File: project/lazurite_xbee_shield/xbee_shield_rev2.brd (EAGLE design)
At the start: 23 x 32.2 mm, 2 parts

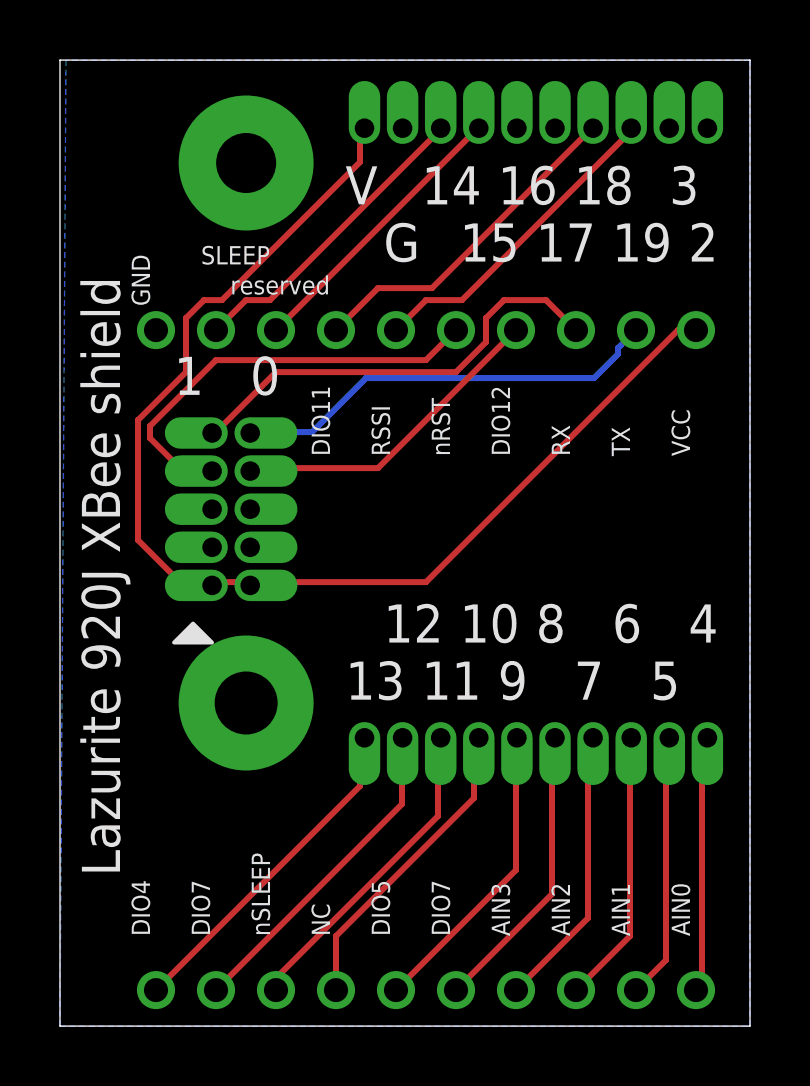
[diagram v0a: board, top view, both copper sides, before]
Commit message: update libraries and all schematic/board data.
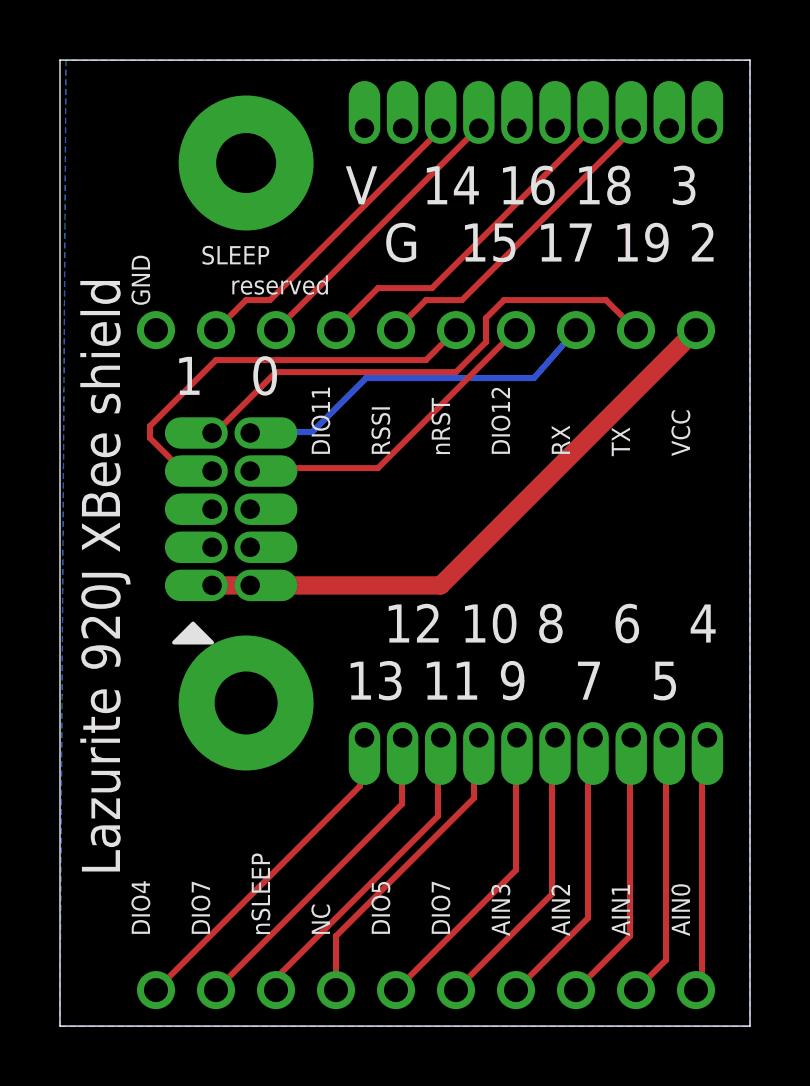
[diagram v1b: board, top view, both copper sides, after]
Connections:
- net 0: now also XB1.3; no longer XB1.2
- net 1: now also XB1.2; no longer XB1.3
- net VDD: no longer U1.VCC3V_2
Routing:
- net VDD: track 40.1 -> 19.7 mm
- net 0: track 14.4 -> 12.3 mm
- net 1: track 14.8 -> 16.8 mm
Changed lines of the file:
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@@
 </signal>
 <signal name="0">
-<contactref element="XB1" pad="2"/>
 <contactref element="U1" pad="0"/>
 <wire x1="8.4" y1="19.8" x2="6.4" y2="19.8" width="0.2" layer="16"/>
 <wire x1="10.2" y1="21.6" x2="8.4" y2="19.8" width="0.2" layer="16"/>
-<wire x1="17.8" y1="21.6" x2="10.2" y2="21.6" width="0.2" layer="16"/>
-<wire x1="18.6" y1="22.4" x2="17.8" y2="21.6" width="0.2" layer="16"/>
-<wire x1="18.6" y1="22.6" x2="18.6" y2="22.4" width="0.2" layer="16"/>
-<wire x1="19.2" y1="23.2" x2="18.6" y2="22.6" width="0.2" layer="16"/>
+<wire x1="15.8" y1="21.6" x2="10.2" y2="21.6" width="0.2" layer="16"/>
 <wire x1="6.4" y1="19.8" x2="6.34" y2="19.77" width="0.2" layer="16"/>
+<contactref element="XB1" pad="3"/>
+<wire x1="15.8" y1="21.6" x2="17.2" y2="23.2" width="0.2" layer="16"/>
 </signal>
 <signal name="1">
-<contactref element="XB1" pad="3"/>
 <contactref element="U1" pad="1"/>
 <wire x1="7.2" y1="21.8" x2="5.2" y2="19.8" width="0.2" layer="1"/>
@@
 <wire x1="14.2" y1="23.6" x2="14.2" y2="22.8" width="0.2" layer="1"/>
 <wire x1="14.8" y1="24.2" x2="14.2" y2="23.6" width="0.2" layer="1"/>
-<wire x1="16.2" y1="24.2" x2="14.8" y2="24.2" width="0.2" layer="1"/>
-<wire x1="17.2" y1="23.2" x2="16.2" y2="24.2" width="0.2" layer="1"/>
+<wire x1="18.2" y1="24.2" x2="14.8" y2="24.2" width="0.2" layer="1"/>
 <wire x1="5.2" y1="19.8" x2="5.07" y2="19.77" width="0.2" layer="1"/>
+<contactref element="XB1" pad="2"/>
+<wire x1="18.2" y1="24.2" x2="19.2" y2="23.2" width="0.2" layer="1"/>
 </signal>
 <signal name="TEST1N">
@@
 <contactref element="XB1" pad="1"/>
 <contactref element="U1" pad="VCC5V_1"/>
-<contactref element="U1" pad="VCC3V_2"/>
-<wire x1="6.2" y1="14.8" x2="5.2" y2="14.8" width="0.2" layer="1"/>
-<wire x1="5.2" y1="14.8" x2="5.07" y2="14.69" width="0.2" layer="1"/>
-<wire x1="6.2" y1="14.8" x2="6.34" y2="14.69" width="0.2" layer="1"/>
-<wire x1="10" y1="28.8" x2="10" y2="29.8" width="0.2" layer="1"/>
-<wire x1="5.4" y1="24.2" x2="10" y2="28.8" width="0.2" layer="1"/>
-<wire x1="4.8" y1="24.2" x2="5.4" y2="24.2" width="0.2" layer="1"/>
-<wire x1="4.2" y1="23.6" x2="4.8" y2="24.2" width="0.2" layer="1"/>
-<wire x1="4.2" y1="21.8" x2="4.2" y2="23.6" width="0.2" layer="1"/>
-<wire x1="2.6" y1="20.2" x2="4.2" y2="21.8" width="0.2" layer="1"/>
-<wire x1="2.6" y1="16.2" x2="2.6" y2="20.2" width="0.2" layer="1"/>
-<wire x1="4" y1="14.8" x2="2.6" y2="16.2" width="0.2" layer="1"/>
-<wire x1="5" y1="14.8" x2="4" y2="14.8" width="0.2" layer="1"/>
-<wire x1="10" y1="29.8" x2="10.15" y2="29.93" width="0.2" layer="1"/>
-<wire x1="5" y1="14.8" x2="5.07" y2="14.69" width="0.2" layer="1"/>
-<wire x1="20.6" y1="23.2" x2="21.2" y2="23.2" width="0.2" layer="1"/>
-<wire x1="12.2" y1="14.8" x2="20.6" y2="23.2" width="0.2" layer="1"/>
-<wire x1="6.4" y1="14.8" x2="12.2" y2="14.8" width="0.2" layer="1"/>
-<wire x1="6.4" y1="14.8" x2="6.34" y2="14.69" width="0.2" layer="1"/>
+<wire x1="5.07" y1="14.69" x2="6.34" y2="14.69" width="0.6096" layer="1"/>
+<wire x1="6.34" y1="14.69" x2="12.69" y2="14.69" width="0.6096" layer="1"/>
+<wire x1="12.69" y1="14.69" x2="21.2" y2="23.2" width="0.6096" layer="1"/>
 </signal>
 <signal name="TEST0">
